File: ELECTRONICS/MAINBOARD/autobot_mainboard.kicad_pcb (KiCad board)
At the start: 4 copper layers, 268 x 112 mm, 164 parts, among them IC1 DW3210, J1 USB_C_Receptacle_USB2.0_16P, J10 Conn_01x05_Socket, J11 Conn_01x01_Socket, J12 Conn_01x02_Pin, J13 Conn_01x01_Socket, J17 Conn_01x02_Pin, J18 Conn_01x02_Pin, J19 Conn_02x05_Odd_Even, J2 Conn_01x01_Socket, J20 Conn_02x05_Odd_Even, J3 Conn_01x01_Socket, J4 Conn_01x02_Socket, J5 Conn_01x01_Socket, J6 Conn_01x01_Socket, J7 Conn_01x03_Pin, J8 Conn_Coaxial, J9 Conn_Coaxial, Q1 DMG1012T, Q2 DMG1012T, Q3 DMG1012T, Q4 DMG1012T, Q5 DMG1012T, SW1 RESET, SW2 BOOT, SW3 SW_Push, U1 TVS1400DRV, U10 VL53L1X, U11 VL53L1X, U12 VL53L1X, U13 BMI270, U14 BMI270, U16 LP5907MFX-3.3, U18 LP5907MFX-3.3, U19 STM32H743VITx, U2 LMR51430XDDCR, U23 LP5907MFX-3.3, U3 LP5907MFX-3.3, U4 TPD2EUSB30A, U7 STM32G031C_4-6-8_Tx, U9 VL53L1X, Y1 TXC 8Y38472012, Y2 25mhz placeholder

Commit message: stuff on the h743 prelim route
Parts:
- moved SW1 81.9 mm to (211.9, 82.7), turned to 90 degrees
- moved R22 79.9 mm to (219.6, 83.0), turned to 180 degrees
- moved Y2 72.2 mm to (217.9, 78.5), turned to -90 degrees
- moved C57 68.1 mm to (214.2, 81.0), turned to -90 degrees
- moved R21 66.6 mm to (226.5, 68.7), turned to 180 degrees
- moved SW2 66.2 mm to (224.8, 66.7), turned to 180 degrees
- moved C55 65.4 mm to (216.9, 76.4), turned to 180 degrees
- moved C56 62.7 mm to (219.7, 78.7), turned to 90 degrees
- moved C58 51.0 mm to (235.0, 90.0), turned to -90 degrees
- moved C59 41.0 mm to (239.9, 75.0)
- moved C63 15.1 mm to (207.9, 71.0)
- moved C69 15.1 mm to (206.1, 70.5)
- moved C68 2.31 mm to (219.7, 74.8), turned to 180 degrees
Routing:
- net /STM32H743/NRST: track 0.00 -> 10.4 mm
- net /STM32H743/PH0: track 0.00 -> 8.45 mm
- net /STM32H743/BOOT0: track 0.00 -> 5.63 mm
- net /STM32H743/PH1: track 0.00 -> 4.22 mm
- net +3V3: track 95.7 -> 91.8 mm
- net /STM32H743/VREF: track 0.00 -> 2.34 mm
- net Net-(C58-Pad1): track 0.00 -> 1.84 mm
- net Net-(C59-Pad1): track 0.00 -> 1.74 mm
- net Net-(U19-VDDA): track 4.41 -> 5.47 mm

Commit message: .
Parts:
- moved U3 43.3 mm to (236.2, 94.5)
- moved C6 40.6 mm to (238.2, 92.5)
- moved C5 37.4 mm to (234.1, 92.5), turned to 180 degrees
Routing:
- net +5V: track 101.2 -> 102.5 mm
- net +3V3: track 91.8 -> 93.1 mm
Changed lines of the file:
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@@
 	(footprint "Package_TO_SOT_SMD:SOT-23-5"
 		(layer "F.Cu")
-		(at 195.55 79.445)
+		(at 236.1625 94.55)
 		(descr "SOT, 5 Pin (JEDEC MO-178 Var AA https://www.jedec.org/document_search?search_api_views_fulltext=MO-178)")
 		(tags "SOT TO_SOT_SMD")
@@
 	(footprint "Capacitor_SMD:C_0402_1005Metric"
 		(layer "F.Cu")
-		(at 199.56 80)
+		(at 238.2 92.5)
 		(descr "Capacitor SMD 0402 (1005 Metric), square (rectangular) end terminal, IPC-7351 nominal, (Body size source: IPC-SM-782 page 76, https://www.pcb-3d.com/wordpress/wp-content/uploads/ipc-sm-782a_amendment_1_and_2.pdf)")
 		(tags "capacitor")
@@
 	(footprint "Capacitor_SMD:C_0402_1005Metric"
 		(layer "F.Cu")
-		(at 199.56 78.03)
+		(at 234.1 92.5 180)
 		(descr "Capacitor SMD 0402 (1005 Metric), square (rectangular) end terminal, IPC-7351 nominal, (Body size source: IPC-SM-782 page 76, https://www.pcb-3d.com/wordpress/wp-content/uploads/ipc-sm-782a_amendment_1_and_2.pdf)")
 		(tags "capacitor")
@@
 		(duplicate_pad_numbers_are_jumpers no)
 		(fp_line
-			(start -0.107836 -0.36)
-			(end 0.107836 -0.36)
+			(start -0.107836 0.36)
+			(end 0.107836 0.36)
 			(stroke
 				(width 0.12)
@@
 		)
 		(fp_line
-			(start -0.107836 0.36)
-			(end 0.107836 0.36)
+			(start -0.107836 -0.36)
+			(end 0.107836 -0.36)
 			(stroke
 				(width 0.12)
@@
 		)
 		(pad "1" smd roundrect
-			(at -0.48 0)
+			(at -0.48 0 180)
 			(size 0.56 0.62)
 			(layers "F.Cu" "F.Mask" "F.Paste")
@@
 		)
 		(pad "2" smd roundrect
-			(at 0.48 0)
+			(at 0.48 0 180)
 			(size 0.56 0.62)
 			(layers "F.Cu" "F.Mask" "F.Paste")
@@
 	)
 	(segment
+		(start 237.3 93.3)
+		(end 237.3 93.6)
+		(width 0.2)
+		(layer "F.Cu")
+		(net "+3V3")
+	)
+	(segment
 		(start 225.239314 46.280686)
 		(end 225.239314 46.285)
@@
 	)
 	(segment
+		(start 237.72 92.5)
+		(end 237.72 92.88)
+		(width 0.2)
+		(layer "F.Cu")
+		(net "+3V3")
+	)
+	(segment
 		(start 242.55 58.15)
 		(end 242.1 58.6)
@@
 	)
 	(segment
+		(start 237.72 92.88)
+		(end 237.3 93.3)
+		(width 0.2)
+		(layer "F.Cu")
+		(net "+3V3")
+	)
+	(segment
 		(start 227.1 47.175)
 		(end 226.475 47.175)
@@
 	)
 	(segment
+		(start 235.025 93.325)
+		(end 235.025 93.6)
+		(width 0.2)
+		(layer "F.Cu")
+		(net "+5V")
+	)
+	(segment
 		(start 24.4 46.2875)
 		(end 27.6425 46.2875)
@@
 	)
 	(segment
+		(start 234.58 92.5)
+		(end 234.58 92.88)
+		(width 0.2)
+		(layer "F.Cu")
+		(net "+5V")
+	)
+	(segment
 		(start 337.697499 83.3)
 		(end 337.697499 84.382501)
 		(width 0.2)
 		(layer "F.Cu")
+		(net "+5V")
+	)
+	(segment
+		(start 234.58 92.88)
+		(end 235.025 93.325)
+		(width 0.2)
+		(layer "F.Cu")

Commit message: reminder to fix power
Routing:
- net +3V3: track 93.1 -> 79.6 mm
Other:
- board text added: "REDO POWER"
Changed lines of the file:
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@@
 		)
 	)
+	(gr_text "REDO POWER"
+		(at 11.75 50.5 0)
+		(layer "Dwgs.User")
+		(effects
+			(font
+				(size 5 5)
+			)
+			(justify left bottom)
+		)
+	)
 	(segment
 		(start 239.3 50.725)
@@
 	)
 	(segment
-		(start 37.9 37.9)
-		(end 37.9 34.194251)
-		(width 0.5)
-		(layer "In2.Cu")
-		(net "+3V3")
-	)
-	(segment
 		(start 30.55 31.8)
 		(end 37.55 31.8)
@@
 	)
 	(segment
-		(start 37.9 34.194251)
-		(end 38.55 33.544251)
-		(width 0.5)
-		(layer "In2.Cu")
-		(net "+3V3")
-	)
-	(segment
-		(start 38.55 33.544251)
-		(end 38.55 30.05)
-		(width 0.5)
-		(layer "In2.Cu")
-		(net "+3V3")
-	)
-	(segment
-		(start 41.725 41.725)
-		(end 37.9 37.9)
-		(width 0.5)
-		(layer "In2.Cu")
-		(net "+3V3")
-	)
-	(segment
 		(start 37.55 31.8)
 		(end 38.05 31.3)
@@
 	)
 	(segment
-		(start 338.1975 84.2975)
-		(end 338.4 84.5)
-		(width 0.2)
-		(layer "F.Cu")
-		(net "/BMI270_R/BMI_INT")
-	)
-	(segment
-		(start 338.1975 83.3)
-		(end 338.1975 84.2975)
-		(width 0.2)
-		(layer "F.Cu")
-		(net "/BMI270_R/BMI_INT")
-	)
-	(segment
-		(start 337.697499 79.602501)
-		(end 337.7 79.6)
-		(width 0.2)
-		(layer "F.Cu")
-		(net "/BMI270_R/BMI_INT")
-	)
-	(segment
-		(start 337.697499 80.887)
-		(end 337.697499 79.602501)
-		(width 0.2)
-		(layer "F.Cu")
-		(net "/BMI270_R/BMI_INT")
-	)
-	(via
-		(at 338.4 84.5)
-		(size 0.6)
-		(drill 0.3)
-		(layers "F.Cu" "B.Cu")
-		(net "/BMI270_R/BMI_INT")
-	)
-	(segment
-		(start 335.8 83.8)
-		(end 335.8 79.9)
-		(width 0.2)
-		(layer "B.Cu")
-		(net "/BMI270_R/BMI_INT")
-	)
-	(segment
-		(start 338.4 84.5)
-		(end 336.5 84.5)
-		(width 0.2)
-		(layer "B.Cu")
-		(net "/BMI270_R/BMI_INT")
-	)
-	(segment
-		(start 336.5 84.5)
-		(end 335.8 83.8)
-		(width 0.2)
-		(layer "B.Cu")
-		(net "/BMI270_R/BMI_INT")
-	)
-	(segment
 		(start 223.8 48.94)
 		(end 223.8 49.475)
@@
 	)
 	(segment
-		(start 350.95 83.804)
-		(end 351.1525 84.0065)
-		(width 0.2)
-		(layer "F.Cu")
-		(net "/BMI270_L/BMI_INT")
-	)
-	(segment
-		(start 350.449999 79.109001)
-		(end 350.4525 79.1065)
-		(width 0.2)
-		(layer "F.Cu")
-		(net "/BMI270_L/BMI_INT")
-	)
-	(segment
-		(start 350.95 82.8065)
-		(end 350.95 83.804)
-		(width 0.2)
-		(layer "F.Cu")
-		(net "/BMI270_L/BMI_INT")
-	)
-	(segment
-		(start 350.449999 80.3935)
-		(end 350.449999 79.109001)
-		(width 0.2)
-		(layer "F.Cu")
-		(net "/BMI270_L/BMI_INT")
-	)
-	(via
-		(at 351.1525 84.0065)
-		(size 0.6)
-		(drill 0.3)
-		(layers "F.Cu" "B.Cu")
-		(net "/BMI270_L/BMI_INT")
-	)
-	(segment
-		(start 348.5525 83.3065)
-		(end 348.5525 79.4065)
-		(width 0.2)
-		(layer "B.Cu")
-		(net "/BMI270_L/BMI_INT")
-	)
-	(segment
-		(start 349.2525 84.0065)
-		(end 348.5525 83.3065)
-		(width 0.2)
-		(layer "B.Cu")
-		(net "/BMI270_L/BMI_INT")
-	)
-	(segment
-		(start 351.1525 84.0065)
-		(end 349.2525 84.0065)
-		(width 0.2)
-		(layer "B.Cu")
-		(net "/BMI270_L/BMI_INT")
-	)
-	(segment
 		(start 264.6781 117.785999)
 		(end 263.116 117.785999)
@@
 	)
 	(segment
+		(start 338.1975 84.2975)
+		(end 338.4 84.5)
+		(width 0.2)
+		(layer "F.Cu")
+		(net "/BMI270_R/BMI_INT")
+	)
+	(segment
+		(start 338.1975 83.3)
+		(end 338.1975 84.2975)
+		(width 0.2)
+		(layer "F.Cu")
+		(net "/BMI270_R/BMI_INT")
+	)
+	(segment
+		(start 337.697499 79.602501)
+		(end 337.7 79.6)
+		(width 0.2)
+		(layer "F.Cu")
+		(net "/BMI270_R/BMI_INT")
+	)
+	(segment
+		(start 337.697499 80.887)
+		(end 337.697499 79.602501)
+		(width 0.2)
+		(layer "F.Cu")
+		(net "/BMI270_R/BMI_INT")
+	)
+	(via
+		(at 338.4 84.5)
+		(size 0.6)
+		(drill 0.3)
+		(layers "F.Cu" "B.Cu")
+		(net "/BMI270_R/BMI_INT")
+	)
+	(segment
+		(start 335.8 83.8)
+		(end 335.8 79.9)
+		(width 0.2)
+		(layer "B.Cu")
+		(net "/BMI270_R/BMI_INT")
+	)
+	(segment
+		(start 338.4 84.5)
+		(end 336.5 84.5)
+		(width 0.2)
+		(layer "B.Cu")
+		(net "/BMI270_R/BMI_INT")
+	)
+	(segment
+		(start 336.5 84.5)
+		(end 335.8 83.8)
+		(width 0.2)
+		(layer "B.Cu")
+		(net "/BMI270_R/BMI_INT")
+	)
+	(segment
 		(start 341.193499 82.593499)
 		(end 341.2 82.6)
@@
 	)
 	(segment
+		(start 350.95 83.804)
+		(end 351.1525 84.0065)
+		(width 0.2)
+		(layer "F.Cu")
+		(net "/BMI270_L/BMI_INT")
+	)
+	(segment
+		(start 350.449999 79.109001)
+		(end 350.4525 79.1065)
+		(width 0.2)
+		(layer "F.Cu")
+		(net "/BMI270_L/BMI_INT")
+	)
+	(segment
+		(start 350.95 82.8065)
+		(end 350.95 83.804)
+		(width 0.2)
+		(layer "F.Cu")
+		(net "/BMI270_L/BMI_INT")
+	)
+	(segment
+		(start 350.449999 80.3935)
+		(end 350.449999 79.109001)
+		(width 0.2)
+		(layer "F.Cu")
+		(net "/BMI270_L/BMI_INT")
+	)
+	(via
+		(at 351.1525 84.0065)
+		(size 0.6)
+		(drill 0.3)
+		(layers "F.Cu" "B.Cu")
+		(net "/BMI270_L/BMI_INT")
+	)
+	(segment
+		(start 348.5525 83.3065)
+		(end 348.5525 79.4065)
+		(width 0.2)
+		(layer "B.Cu")
+		(net "/BMI270_L/BMI_INT")
+	)
+	(segment
+		(start 349.2525 84.0065)
+		(end 348.5525 83.3065)
+		(width 0.2)
+		(layer "B.Cu")
+		(net "/BMI270_L/BMI_INT")
+	)
+	(segment
+		(start 351.1525 84.0065)
+		(end 349.2525 84.0065)
+		(width 0.2)
+		(layer "B.Cu")
+		(net "/BMI270_L/BMI_INT")
+	)
+	(segment

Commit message: changed power plane, do gnd stitching soon
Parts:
- removed J10: Conn_01x05_Socket, Connector_PinHeader_2.54mm:PinHeader_1x05_P2.54mm_Vertical
- moved U4 94.1 mm to (230.5, 101.5)
- moved C27 85.1 mm to (263.5, 69.8)
- moved C28 85.1 mm to (265.2, 72.6)
- moved C29 85.1 mm to (250.8, 70.3)
- moved C30 85.1 mm to (252.4, 73.1)
- moved U13 85.1 mm to (266.9, 69.8)
- moved U14 85.1 mm to (254.2, 70.3)
- moved R21 62.5 mm to (164.9, 57.8)
- moved SW2 62.5 mm to (163.2, 55.8)
- moved J1 56.3 mm to (230.0, 108.8)
- moved C1 52.0 mm to (308.5, 151.7)
- moved R1 52.0 mm to (313.5, 146.9)
- moved C3 52.0 mm to (309.8, 143.0)
- moved L1 52.0 mm to (296.8, 146.7)
- moved R2 52.0 mm to (313.5, 148.5)
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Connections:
- R5 pad 1: /USB/DATA - -> /USB/DATA +
- R6 pad 1: /USB/DATA + -> /USB/DATA -
- U4 pad 1: /USB/DATA + -> /USB/DATA -
- U4 pad 2: /USB/DATA - -> /USB/DATA +
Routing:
- net +24V: track 7.77 -> 59.9 mm
- net /USB/DATA +: track 0.00 -> 16.4 mm
- net /USB/DATA -: track 0.00 -> 16.4 mm
- net +3V3: track 79.6 -> 92.9 mm
- net /STM32G0/DRVOFF_R: track 14.0 -> 15.7 mm
- net /LMR51430XDDCR/12V: track 6.90 -> 8.29 mm
- net Net-(U2-SW): track 13.1 -> 14.1 mm
- net /STM32G0/SDA: track 22.6 -> 22.0 mm
- net GNDREF: track 65.8 -> 65.7 mm, vias 59 -> 57

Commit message: power zone
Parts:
- moved R6 80.9 mm to (241.8, 76.9), turned to 180 degrees
- moved R5 80.6 mm to (241.8, 75.9), turned to 180 degrees
- moved U18 69.5 mm to (224.8, 59.5), turned to 90 degrees
- moved C3 66.5 mm to (250.3, 113.4)
- moved L1 66.5 mm to (237.3, 117.1)
- moved C1 66.5 mm to (249.0, 122.1)
- moved R1 66.5 mm to (254.0, 117.3)
- moved R2 66.5 mm to (254.0, 118.9)
- moved C2 66.5 mm to (249.0, 120.7)
- moved U2 66.5 mm to (249.8, 117.1)
- moved U1 66.5 mm to (247.6, 125.7)
- moved C54 66.3 mm to (223.4, 56.7), turned to 180 degrees
- moved C53 62.8 mm to (223.3, 62.2), turned to 180 degrees
- moved C4 58.7 mm to (231.3, 114.0), turned to 180 degrees
- moved J1 41.1 mm to (255.8, 76.8), turned to 90 degrees
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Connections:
- R5 pad 1: /USB/DATA + -> /USB/DATA -
- R5 pad 2: /STM32H743/D- -> /STM32H743/D+
- R6 pad 1: /USB/DATA - -> /USB/DATA +
- R6 pad 2: /STM32H743/D+ -> /STM32H743/D-
- U4 pad 1: /USB/DATA - -> /USB/DATA +
- U4 pad 2: /USB/DATA + -> /USB/DATA -
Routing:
- net /USB/DATA -: track 16.4 -> 5.48 mm
- net +3V3: track 92.9 -> 101.3 mm, vias 20 -> 41
- net /STM32H743/SWDIO: track 0.00 -> 5.54 mm
- net +5V: track 102.5 -> 107.2 mm
- net /USB/DATA +: track 16.4 -> 12.0 mm
- net Net-(C59-Pad1): track 1.74 -> 3.49 mm
- net GNDREF: track 65.7 -> 66.2 mm, vias 57 -> 155
- net /LMR51430XDDCR/12V: vias 2 -> 1
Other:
- board text added: "just fix this later ig, if the trace is short enough, remove r5 r6"

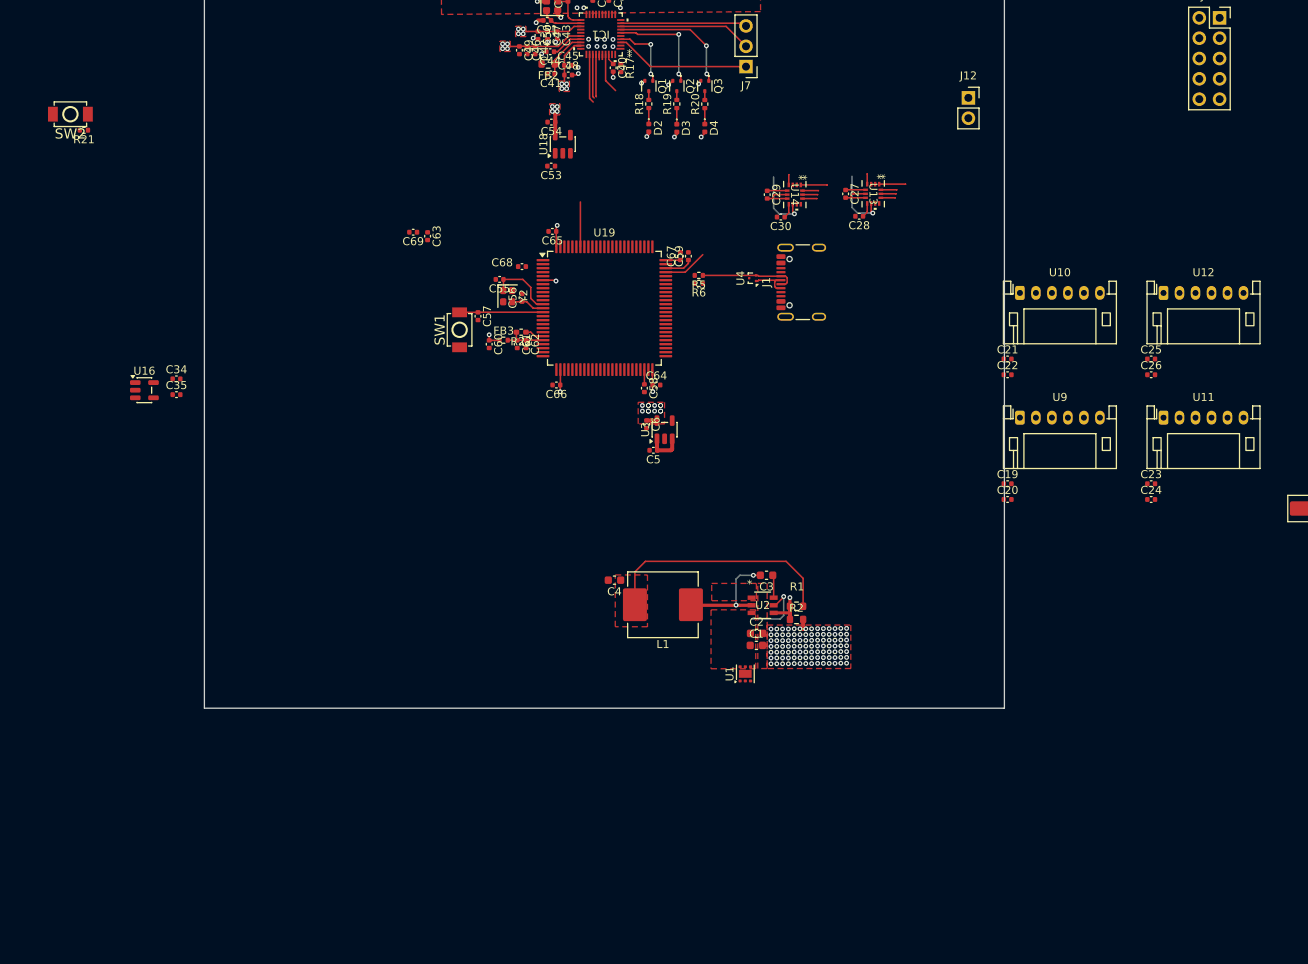
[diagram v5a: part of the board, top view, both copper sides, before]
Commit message: change ToF module connection to use just one bus
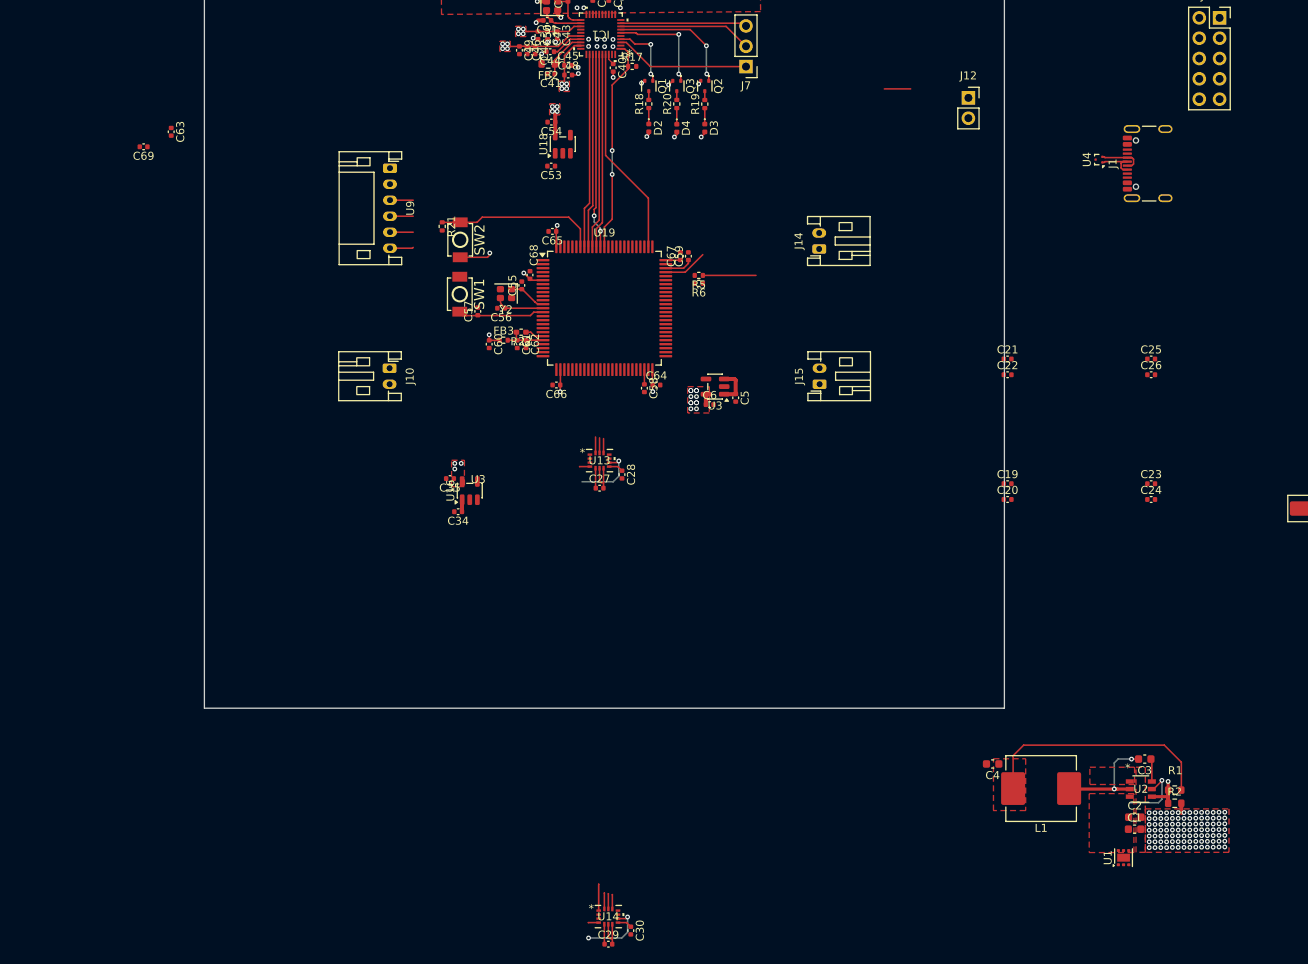
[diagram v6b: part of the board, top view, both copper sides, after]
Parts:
- removed U10, U11, U12: VL53L1X, Connector_JST:JST_PH_S6B-PH-K_1x06_P2.00mm_Horizontal
- added J10: Conn_01x02_Pin, Connector_JST:JST_PH_S2B-PH-K_1x02_P2.00mm_Horizontal, F.Cu at (203.2, 87.5)
- added J14: Conn_01x02_Pin, Connector_JST:JST_PH_S2B-PH-K_1x02_P2.00mm_Horizontal, F.Cu at (256.9, 72.6)
- added J15: Conn_01x02_Pin, Connector_JST:JST_PH_S2B-PH-K_1x02_P2.00mm_Horizontal, F.Cu at (256.9, 89.5)
- moved C29 95.8 mm to (230.5, 159.5), turned to 0 degrees
- moved U14 93.2 mm to (230.5, 156.1), turned to 0 degrees
- moved C30 91.1 mm to (233.3, 157.8), turned to -90 degrees
- moved U9 84.7 mm to (203.2, 62.5), turned to -90 degrees
- moved C1 52.6 mm to (296.3, 145.1)
- moved C3 52.6 mm to (297.5, 136.4)
- moved C4 52.6 mm to (278.5, 137.0)
- moved U2 52.6 mm to (297.1, 140.1)
- moved C2 52.6 mm to (296.3, 143.6)
- moved L1 52.6 mm to (284.6, 140.0)
- moved U1 52.6 mm to (294.9, 148.7)
- moved R1 52.6 mm to (301.3, 140.2)
- moved R2 52.6 mm to (301.3, 141.9)
- moved SW2 51.2 mm to (212.0, 71.5), turned to -90 degrees
- moved C27 48.0 mm to (229.4, 102.5), turned to 0 degrees
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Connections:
- U13 pad 9: /BMI270_L/BMI_INT -> /BMI270_L/BMI_INT2
- U14 pad 9: /BMI270_R/BMI_INT -> /BMI270_R/BMI_INT2
- U19 pad 1: /STM32H743/INDEX_L -> unconnected-(U19-PE2-Pad1)
- U19 pad 2: /STM32H743/DIAG_L -> unconnected-(U19-PE3-Pad2)
- U19 pad 77: unconnected-(U19-PA15-Pad77) -> /DW3220_T/CSN
- U19 pad 88: unconnected-(U19-PD7-Pad88) -> /DW3220_T/IRQ
- U19 pad 89: unconnected-(U19-PB3-Pad89) -> /DW3220_T/SPICLK
- U19 pad 90: unconnected-(U19-PB4-Pad90) -> /DW3220_T/MISO
- U19 pad 91: unconnected-(U19-PB5-Pad91) -> /DW3220_T/MOSI
- U19 pad 92: unconnected-(U19-PB6-Pad92) -> /DW3220_T/RESET
- U19 pad 93: unconnected-(U19-PB7-Pad93) -> /DW3220_T/WAKEUP
- U19 pad 97: /STM32H743/RXD0 -> unconnected-(U19-PE0-Pad97)
- U19 pad 98: /STM32H743/TXD0 -> unconnected-(U19-PE1-Pad98)
- U9 pad 5: /STM32H743/VL_IO_0 -> unconnected-(U9-GPIO-Pad5)
- U9 pad 6: /STM32H743/VL_XSHUT_0 -> unconnected-(U9-XSHUT-Pad6)
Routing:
- net (no net): track 29.4 -> 0.00 mm, vias 4 -> 3
- net /DW3220_T/IRQ: track 0.00 -> 26.7 mm, vias 0 -> 2
- net /DW3220_T/MISO: track 0.62 -> 24.4 mm
- net /DW3220_T/MOSI: track 0.73 -> 24.5 mm
- net /DW3220_T/CSN: track 5.09 -> 26.3 mm
- net /DW3220_T/SPICLK: track 5.37 -> 24.5 mm, vias 0 -> 2
- net /DW3220_T/RESET: track 5.57 -> 24.3 mm
- net /DW3220_T/WAKEUP: track 6.19 -> 24.4 mm
- net /DW3220_T/TXLED: track 0.00 -> 16.1 mm, vias 0 -> 2
- net /STM32H743/BOOT0: track 5.63 -> 20.4 mm
- net /DW3220_T/RXLED: track 0.00 -> 13.3 mm, vias 0 -> 2
- net /BMI270_R/BMI_INT2: track 0.00 -> 8.37 mm, vias 0 -> 2
- net /BMI270_L/BMI_INT2: track 0.00 -> 8.07 mm, vias 0 -> 1
- net /BMI270_L/BMI_INT: track 9.36 -> 1.29 mm, vias 1 -> 0
- net /BMI270_R/BMI_INT: track 9.36 -> 1.29 mm, vias 1 -> 0
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- added copper zone on F.Cu, net /LDO3/3V3
- added copper zone on In2.Cu, net /LDO3/3V3
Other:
- board text added: "U3"

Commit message: 10/24 save
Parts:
- removed C5, C6: 1u, Capacitor_SMD:C_0402_1005Metric
- removed U3: LP5907MFX-3.3, Package_TO_SOT_SMD:SOT-23-5
- added C21: 1u, Capacitor_SMD:C_0402_1005Metric, F.Cu at (238.5, 102.5)
- added C22: 1u, Capacitor_SMD:C_0402_1005Metric, F.Cu at (236.2, 102.5)
- added U15: NCP1117-3.3_SOT223, Package_TO_SOT_SMD:SOT-223-3_TabPin2, F.Cu at (235.7, 97.5)
- added U18: LP5907MFX-3.3, Package_TO_SOT_SMD:SOT-23-5, F.Cu at (311.7, 125.0)
- added U23: LP5907MFX-3.3, Package_TO_SOT_SMD:SOT-23-5, F.Cu at (311.7, 131.7)
- moved U1 59.0 mm to (248.6, 112.2), turned to 0 degrees
- moved C35 56.6 mm to (250.6, 141.4)
- moved U16 56.6 mm to (253.1, 142.9)
- moved C34 56.6 mm to (251.7, 145.5)
- moved C1 54.3 mm to (252.1, 113.6), turned to -90 degrees
- moved C2 52.2 mm to (253.6, 113.6), turned to -90 degrees
- moved R2 51.5 mm to (255.4, 118.6), turned to -90 degrees
- moved R1 49.3 mm to (257.0, 118.6), turned to 90 degrees
- moved U2 47.5 mm to (257.1, 114.4), turned to -90 degrees
- moved L1 47.0 mm to (257.2, 101.9), turned to 90 degrees
- moved C4 45.0 mm to (260.3, 95.8), turned to 90 degrees
- moved C3 42.5 mm to (260.9, 114.9), turned to 90 degrees
- moved J10 25.0 mm to (203.2, 62.5)
- moved U9 25.0 mm to (203.2, 87.5)
- moved C28 8.22 mm to (232.8, 109.0)
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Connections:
- C19 pad 1: /LDO3/3V3 -> +3V3
- C20 pad 1: /LDO3/3V3 -> +3V3
- U19 pad 41: unconnected-(U19-PE11-Pad41) -> /BMI270_L/BMI_CS
- U19 pad 42: unconnected-(U19-PE12-Pad42) -> /BMI270_L/BMI_SCK
- U19 pad 43: unconnected-(U19-PE13-Pad43) -> /BMI270_L/BMI_MISO
- U19 pad 44: unconnected-(U19-PE14-Pad44) -> /BMI270_L/BMI_MOSI
- U9 pad 1: /LDO3/3V3 -> +3V3
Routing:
- net /BMI270_L/BMI_INT2: track 8.07 -> 31.3 mm, vias 1 -> 2
- net +3V3: track 106.5 -> 128.0 mm, vias 42 -> 46
- net /BMI270_L/BMI_INT: track 1.29 -> 21.3 mm
- net /BMI270_L/BMI_CS: track 1.79 -> 17.2 mm
- net /BMI270_L/BMI_SCK: track 1.89 -> 17.2 mm
- net /BMI270_L/BMI_MOSI: track 1.99 -> 17.2 mm
- net /BMI270_L/BMI_MISO: track 3.29 -> 16.9 mm
- net +5V: track 108.7 -> 122.3 mm
- net unconnected-(U9-XSHUT-Pad6): track 2.94 -> 0.00 mm
- net unconnected-(U9-GPIO-Pad5): track 2.90 -> 0.00 mm
- net /STM32H743/VL_SDA_0: track 2.90 -> 0.00 mm
- net /STM32H743/VL_SCL_0: track 2.90 -> 0.00 mm
- net GNDREF: vias 155 -> 106
- removed copper zone on F.Cu, net /LDO3/3V3
- removed copper zone on In2.Cu, net /LDO3/3V3
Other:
- board size 268 x 112 mm -> 253 x 112 mm
